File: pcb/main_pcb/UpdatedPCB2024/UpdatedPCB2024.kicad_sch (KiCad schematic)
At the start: 29 parts, among them J1 Conn_01x05, J2 Conn_01x05, J3 Conn_01x05, J4 Conn_01x05, J5 Conn_01x05, J6 Conn_01x05, J7 Conn_01x05, J8 Conn_01x06_Male, J9 Conn_01x06_Male, Q1 Q_NJFET_DSG, Q2 Q_NJFET_DSG, U1 Teensy_4.0, U2 DRV8833, U3 LM3151/2/3

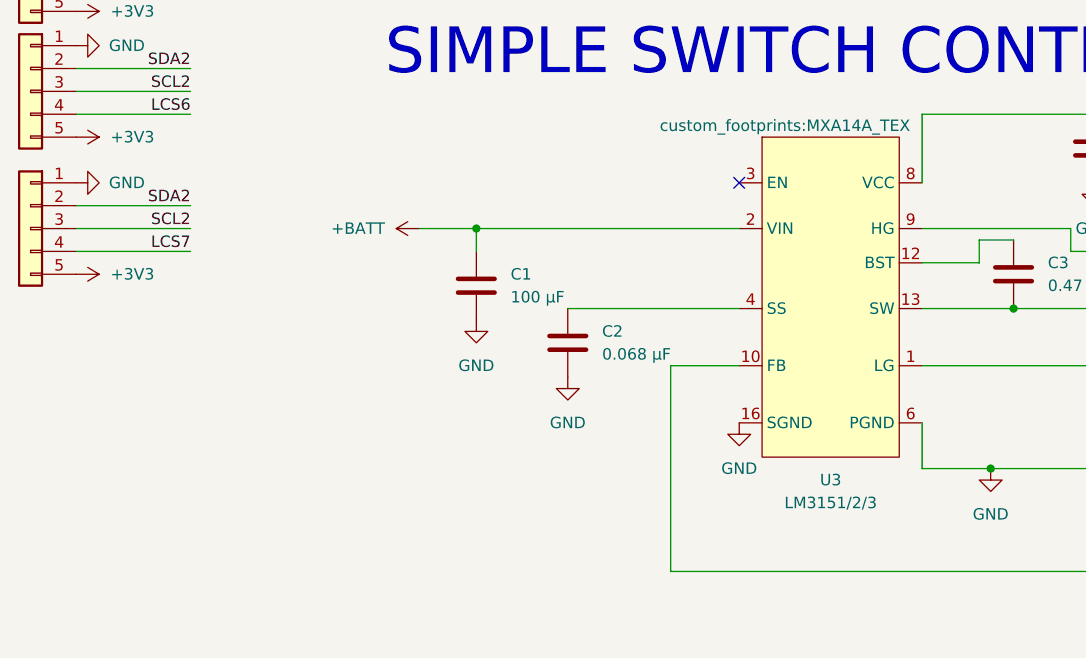
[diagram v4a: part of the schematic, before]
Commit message: fixing errors on PCB as well as readjustments to outline of PCB
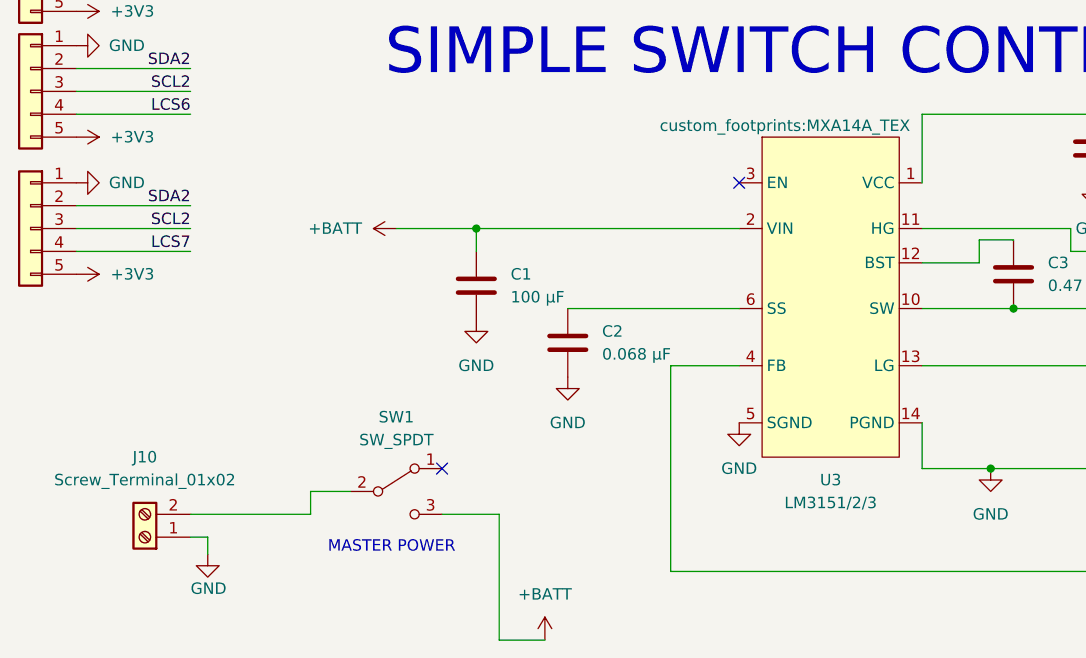
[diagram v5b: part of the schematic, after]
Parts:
- added J10: Screw_Terminal_01x02, TerminalBlock:TerminalBlock_bornier-2_P5.08mm, symbol Connector:Screw_Terminal_01x02
- added SW1: SW_SPDT, custom_footprints:SW_SPDT_NKK_MS12AANW03, symbol Switch:SW_SPDT
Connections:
- net +BATT: now also SW1.3 (C)
- net GND: now also U3.14 (PGND), U3.5 (SGND), J10.1 (Pin_1); no longer U3.16 (SGND), U3.6 (PGND)
- net at C4.1: now also U3.1 (VCC); no longer U3.8 (VCC)
- net at Q2.3 (G): now also U3.13 (LG); no longer U3.1 (LG)
- net at C6.1, L1.1: now also U3.4 (FB); no longer U3.10 (FB)
- net at C3.2, L1.2, Q1.2 (S)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: now also U3.10 (SW); no longer U3.13 (SW)
- net at C2.1: now also U3.6 (SS); no longer U3.4 (SS)
- net at Q1.3 (G): now also U3.11 (HG); no longer U3.9 (HG)
- new net: J10.2 (Pin_2), SW1.2 (B)
- no-connect marks 15 -> 16
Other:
- note added: "MASTER POWER"
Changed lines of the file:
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@@
   )
   (no_connect (at 226.06 140.97))
+  (no_connect (at 68.58 147.32))
   (no_connect (at 101.6 115.57))
   (no_connect (at 139.065 46.355))
@@
     (stroke (width 0) (type default))
   )
+  (wire (pts (xy 74.93 152.4) (xy 74.93 166.37))
+    (stroke (width 0) (type default))
+  )
   (wire (pts (xy 85.725 57.785) (xy 88.9 57.785))
     (stroke (width 0) (type default))
@@
     (stroke (width 0) (type default))
   )
+  (wire (pts (xy 68.58 152.4) (xy 74.93 152.4))
+    (stroke (width 0) (type default))
+  )
   (wire (pts (xy 139.065 56.515) (xy 128.905 56.515))
     (stroke (width 0) (type default))
@@
     (stroke (width 0) (type default))
   )
+  (wire (pts (xy 42.545 154.94) (xy 42.545 156.845))
+    (stroke (width 0) (type default))
+  )
+  (wire (pts (xy 53.975 149.86) (xy 58.42 149.86))
+    (stroke (width 0) (type default))
+  )
   (wire (pts (xy 27.94 33.02) (xy 40.64 33.02))
     (stroke (width 0) (type default))
@@
     (stroke (width 0) (type default))
   )
+  (wire (pts (xy 40.64 154.94) (xy 42.545 154.94))
+    (stroke (width 0) (type default))
+  )
   (wire (pts (xy 121.92 142.24) (xy 121.92 147.32))
     (stroke (width 0) (type default))
@@
     (stroke (width 0) (type default))
   )
+  (wire (pts (xy 74.93 166.37) (xy 80.01 166.37))
+    (stroke (width 0) (type default))
+  )
   (wire (pts (xy 240.03 61.595) (xy 236.22 61.595))
     (stroke (width 0) (type default))
@@
     (stroke (width 0) (type default))
   )
-  (wire (pts (xy 66.04 120.65) (xy 72.39 120.65))
+  (wire (pts (xy 63.5 120.65) (xy 72.39 120.65))
     (stroke (width 0) (type default))
   )
@@
     (stroke (width 0) (type default))
   )
+  (wire (pts (xy 53.975 152.4) (xy 53.975 149.86))
+    (stroke (width 0) (type default))
+  )
   (wire (pts (xy 183.515 51.435) (xy 196.215 51.435))
     (stroke (width 0) (type default))
   )
   (wire (pts (xy 226.06 118.11) (xy 231.14 118.11))
+    (stroke (width 0) (type default))
+  )
+  (wire (pts (xy 40.64 152.4) (xy 53.975 152.4))
     (stroke (width 0) (type default))
   )
@@
   (text "NOTE:\nThe motor control pinout is reveresed for\nmotor B. This means that the same control\nvalue will result in Motor A and Motor B\ngoing in reverse directions. "
     (at 222.885 32.385 0)
+    (effects (font (size 1.27 1.27)) (justify left bottom))
+  )
+  (text "MASTER POWER" (at 55.88 156.845 0)
     (effects (font (size 1.27 1.27)) (justify left bottom))
   )
@@
     )
   )
+  (symbol (lib_id "Switch:SW_SPDT") (at 63.5 149.86 0) (unit 1)
+    (in_bom yes) (on_board yes) (dnp no) (fields_autoplaced)
+    (property "Reference" "SW1" (at 63.5 141.605 0)
+      (effects (font (size 1.27 1.27)))
+    )
+    (property "Value" "SW_SPDT" (at 63.5 144.145 0)
+      (effects (font (size 1.27 1.27)))
+    )
+    (property "Footprint" "custom_footprints:SW_SPDT_NKK_MS12AANW03" (at 63.5 149.86 0)
+      (effects (font (size 1.27 1.27)) hide)
+    )
+    (property "Datasheet" "~" (at 63.5 149.86 0)
+      (effects (font (size 1.27 1.27)) hide)
+    )
+    (pin "1")
+    (pin "2")
+    (pin "3")
+    (instances
+      (project "UpdatedPCB2024"
+        (path "/5fc7237d-899a-432a-80a6-13a354218a79"
+          (reference "SW1") (unit 1)
+        )
+      )
+    )
+  )
   (symbol (lib_id "Connector_Generic:Conn_01x05") (at 22.86 63.5 0) (mirror y) (unit 1)
     (in_bom yes) (on_board yes) (dnp no) (fields_autoplaced)
@@
     (pin "12")
     (pin "13")
-    (pin "16")
+    (pin "14")
     (pin "2")
     (pin "3")
     (pin "4")
     (pin "6")
-    (pin "8")
-    (pin "9")
+    (pin "11")
+    (pin "5")
     (instances
       (project "UpdatedPCB2024"
@@
     )
   )
-  (symbol (lib_id "power:+BATT") (at 66.04 120.65 90) (unit 1)
-    (in_bom yes) (on_board yes) (dnp no) (fields_autoplaced)
-    (property "Reference" "#PWR0118" (at 69.85 120.65 0)
-      (effects (font (size 1.27 1.27)) hide)
-    )
-    (property "Value" "+BATT" (at 62.23 120.6499 90)
-      (effects (font (size 1.27 1.27)) (justify left))
-    )
-    (property "Footprint" "" (at 66.04 120.65 0)
-      (effects (font (size 1.27 1.27)) hide)
-    )
-    (property "Datasheet" "" (at 66.04 120.65 0)
+  (symbol (lib_id "Connector:Screw_Terminal_01x02") (at 35.56 154.94 180) (unit 1)
+    (in_bom yes) (on_board yes) (dnp no) (fields_autoplaced)
+    (property "Reference" "J10" (at 35.56 146.05 0)
+      (effects (font (size 1.27 1.27)))
+    )
+    (property "Value" "Screw_Terminal_01x02" (at 35.56 148.59 0)
+      (effects (font (size 1.27 1.27)))
+    )
+    (property "Footprint" "TerminalBlock:TerminalBlock_bornier-2_P5.08mm" (at 35.56 154.94 0)
+      (effects (font (size 1.27 1.27)) hide)
+    )
+    (property "Datasheet" "~" (at 35.56 154.94 0)
+      (effects (font (size 1.27 1.27)) hide)
+    )
+    (pin "1")
+    (pin "2")
+    (instances
+      (project "UpdatedPCB2024"
+        (path "/5fc7237d-899a-432a-80a6-13a354218a79"
+          (reference "J10") (unit 1)
+        )
+      )
+    )
+  )
+  (symbol (lib_id "power:+BATT") (at 63.5 120.65 90) (unit 1)
+    (in_bom yes) (on_board yes) (dnp no) (fields_autoplaced)
+    (property "Reference" "#PWR0118" (at 67.31 120.65 0)
+      (effects (font (size 1.27 1.27)) hide)
+    )
+    (property "Value" "+BATT" (at 59.69 120.6499 90)
+      (effects (font (size 1.27 1.27)) (justify left))
+    )
+    (property "Footprint" "" (at 63.5 120.65 0)
+      (effects (font (size 1.27 1.27)) hide)
+    )
+    (property "Datasheet" "" (at 63.5 120.65 0)
       (effects (font (size 1.27 1.27)) hide)
     )
@@
         (path "/5fc7237d-899a-432a-80a6-13a354218a79"
           (reference "C1") (unit 1)
+        )
+      )
+    )
+  )
+  (symbol (lib_id "power:GND") (at 42.545 156.845 0) (unit 1)
+    (in_bom yes) (on_board yes) (dnp no)
+    (property "Reference" "#PWR02" (at 42.545 163.195 0)
+      (effects (font (size 1.27 1.27)) hide)
+    )
+    (property "Value" "GND" (at 40.64 160.655 0)
+      (effects (font (size 1.27 1.27)) (justify left))
+    )
+    (property "Footprint" "" (at 42.545 156.845 0)
+      (effects (font (size 1.27 1.27)) hide)
+    )
+    (property "Datasheet" "" (at 42.545 156.845 0)
+      (effects (font (size 1.27 1.27)) hide)
+    )
+    (pin "1")
+    (instances
+      (project "UpdatedPCB2024"
+        (path "/5fc7237d-899a-432a-80a6-13a354218a79"
+          (reference "#PWR02") (unit 1)
         )
       )
@@
         )
       )
+    )
+  )
+  (symbol (lib_id "power:+BATT") (at 80.01 166.37 0) (unit 1)
+    (in_bom yes) (on_board yes) (dnp no) (fields_autoplaced)
+    (property "Reference" "#PWR03" (at 80.01 170.18 0)
+      (effects (font (size 1.27 1.27)) hide)
+    )
+    (property "Value" "+BATT" (at 80.01 161.29 0)
+      (effects (font (size 1.27 1.27)))
+    )
+    (property "Footprint" "" (at 80.01 166.37 0)
+      (effects (font (size 1.27 1.27)) hide)
+    )
+    (property "Datasheet" "" (at 80.01 166.37 0)
+      (effects (font (size 1.27 1.27)) hide)
+    )
+    (pin "1")
+    (instances
+      (project "UpdatedPCB2024"
+        (path "/5fc7237d-899a-432a-80a6-13a354218a79"
+          (reference "#PWR03") (unit 1)
+        )
+      )

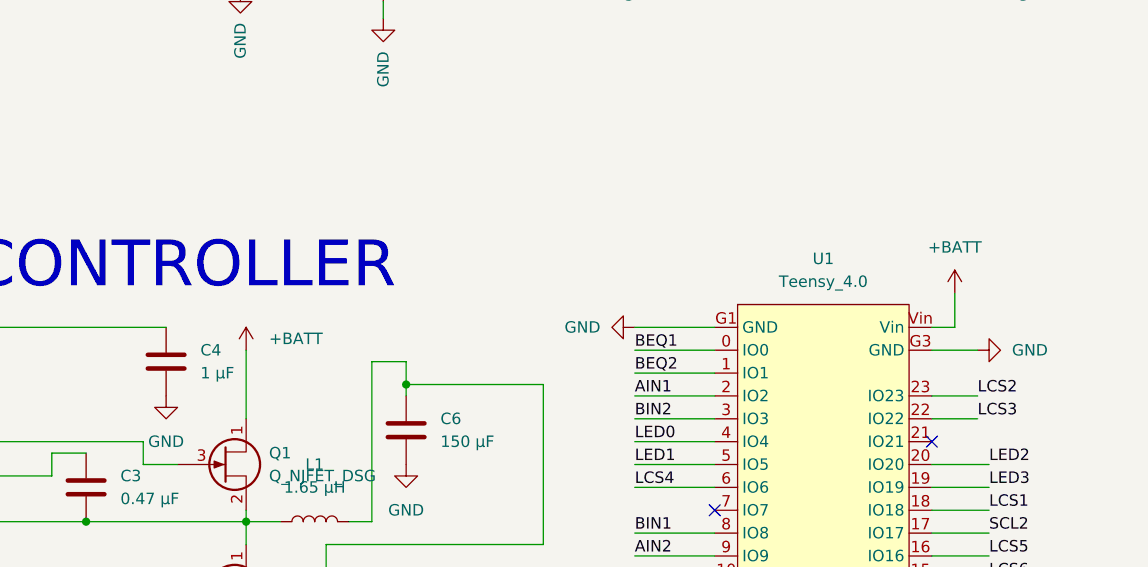
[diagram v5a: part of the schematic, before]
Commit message: Simple switch controller layout
Did the layout for the simple switch controller such that the pathing is easy.
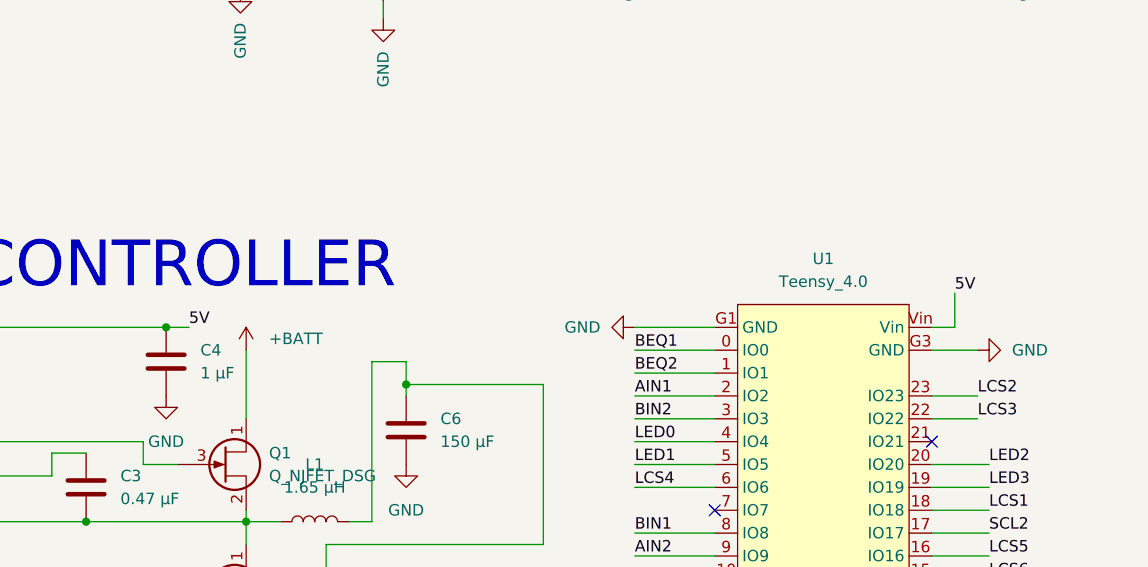
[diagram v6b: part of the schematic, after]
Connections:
- net +BATT: no longer U1.Vin
- net 5V: now reaches C4.1, U3.1 (VCC)
- net 5V: now also U1.Vin

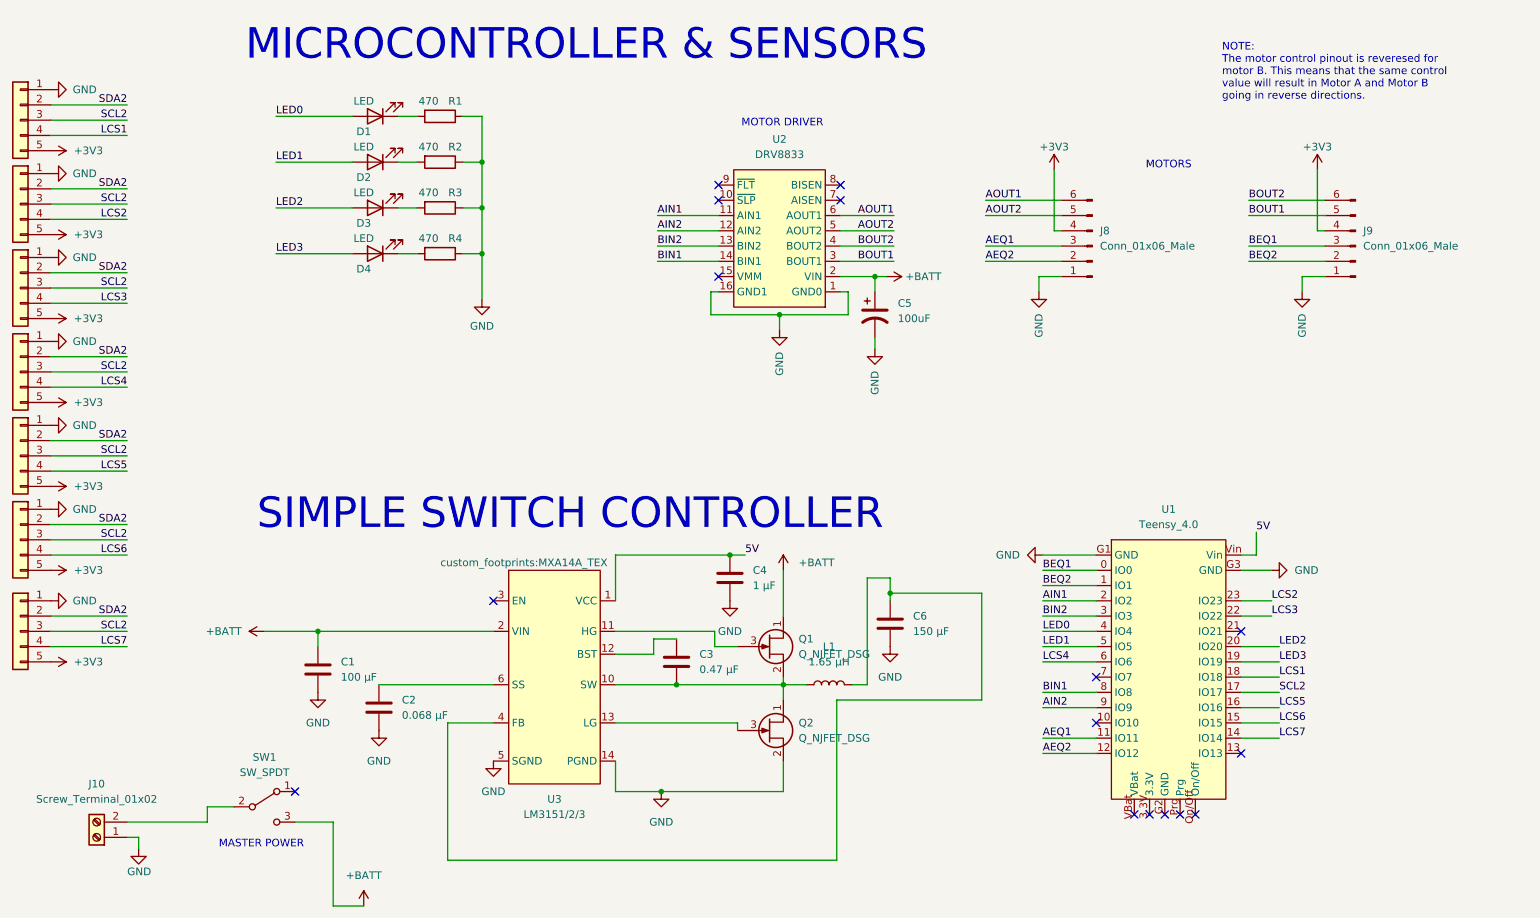
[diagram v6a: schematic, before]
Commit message: Edited schematic + layout
Changed some pin configurations (made sure SDA and SCL are configured properly, as well as all PWM necessary pins) and began routing. Layout at this point is finalized, needs to be reviewed and approved. All LIDARs located on one side of board, and both motor attachments located on the other. Board size is still TBD.
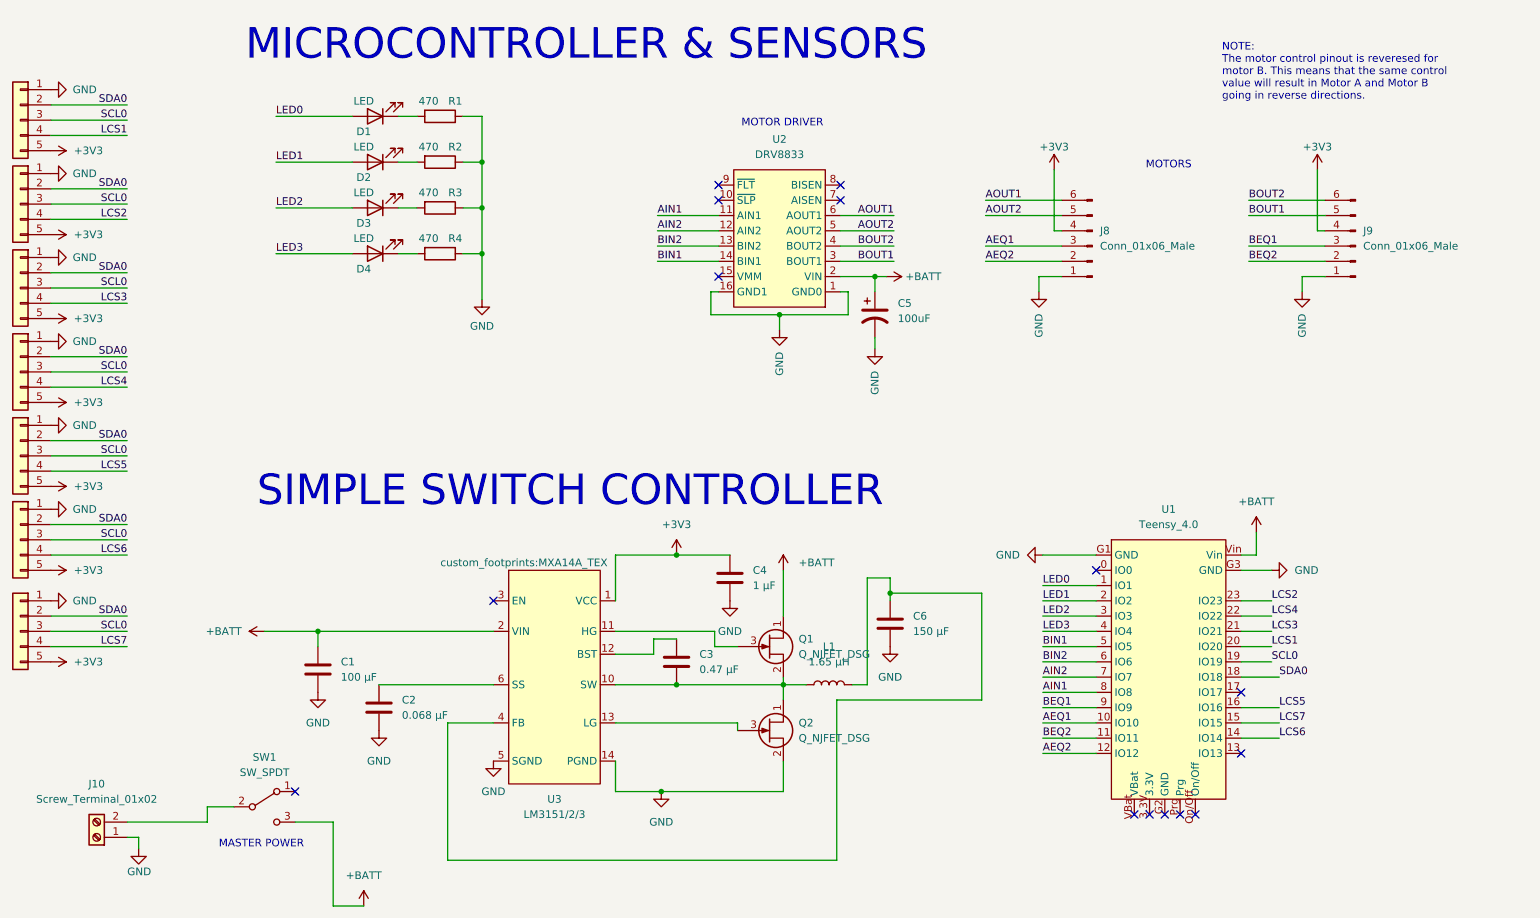
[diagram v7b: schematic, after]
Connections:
- net +3V3: now also C4.1, U3.1 (VCC)
- net +BATT: now also U1.Vin
- net AEQ1: now also U1.10 (IO10); no longer U1.11 (IO11)
- net AIN1: now also U1.8 (IO8); no longer U1.2 (IO2)
- net AIN2: now also U1.7 (IO7); no longer U1.9 (IO9)
- net BEQ1: now also U1.9 (IO9); no longer U1.0 (IO0)
- net BEQ2: now also U1.11 (IO11); no longer U1.1 (IO1)
- net BIN1: now also U1.5 (IO5); no longer U1.8 (IO8)
- net BIN2: now also U1.6 (IO6); no longer U1.3 (IO3)
- net LCS1: now also U1.20 (IO20); no longer U1.18 (IO18)
- net LCS3: now also U1.21 (IO21); no longer U1.22 (IO22)
- net LCS4: now also U1.22 (IO22); no longer U1.6 (IO6)
- net LCS6: now also U1.14 (IO14); no longer U1.15 (IO15)
- net LCS7: now also U1.15 (IO15); no longer U1.14 (IO14)
- net LED0: now also U1.1 (IO1); no longer U1.4 (IO4)
- net LED1: now also U1.2 (IO2); no longer U1.5 (IO5)
- net LED2: now also U1.3 (IO3); no longer U1.20 (IO20)
- net LED3: now also U1.4 (IO4); no longer U1.19 (IO19)
- removed net 5V: C4.1, U1.Vin, U3.1 (VCC)
- net SCL2 renamed SCL0
- net SCL0: now also U1.19 (IO19); no longer U1.17 (IO17)
- net SDA2 renamed SDA0
- net SDA0: now also U1.18 (IO18)
- no-connect marks 16 -> 15
